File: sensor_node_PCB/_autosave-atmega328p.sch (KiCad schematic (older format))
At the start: 11 parts, among them U5 ATmega328P-AU, Y1 Crystal

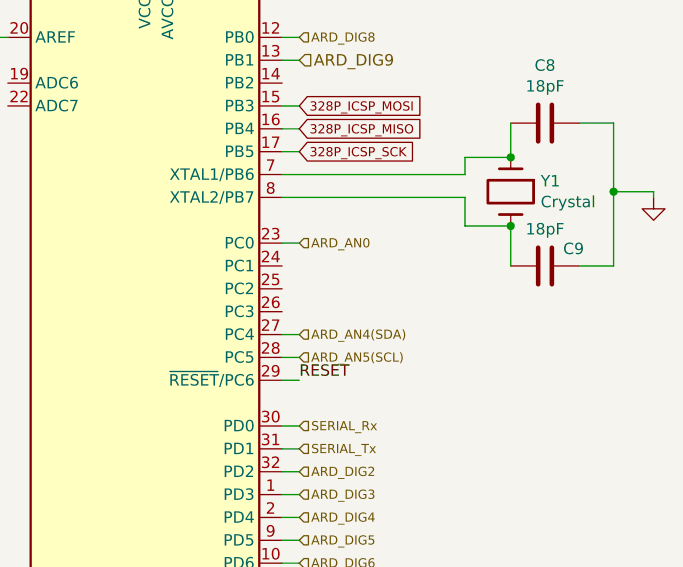
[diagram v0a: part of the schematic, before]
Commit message: made term block silk invisible
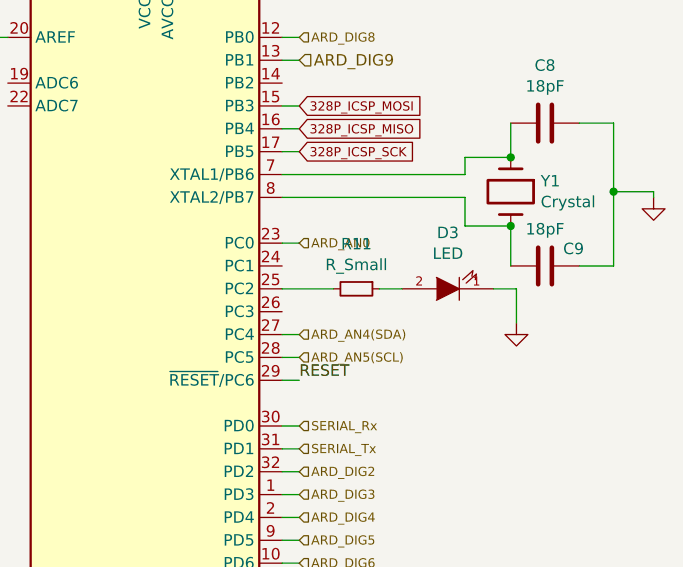
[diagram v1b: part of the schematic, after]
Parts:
- added D3: LED, LED_SMD:LED_0603_1608Metric, symbol Arduino_Uno_R3_From_Scratch-rescue:LED
- added R11: R_Small, LED_SMD:LED_0603_1608Metric, symbol Device:R_Small
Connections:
- net GND: now also D3.1 (K)
- net at U5.25 (PC2): now also R11.2
- new net: D3.2 (A), R11.1
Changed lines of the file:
@@
 Wire Wire Line
 	3625 2050 5325 2050
+$Comp
+L Device:R_Small R11
+U 1 1 5FF88592
+P 8075 4325
+F 0 "R11" V 7879 4325 50  0000 C CNN
+F 1 "R_Small" V 7970 4325 50  0000 C CNN
+F 2 "LED_SMD:LED_0603_1608Metric" H 8075 4325 50  0001 C CNN
+F 3 "~" H 8075 4325 50  0001 C CNN
+	1    8075 4325
+	0    1    1    0
+$EndComp
+$Comp
+L Arduino_Uno_R3_From_Scratch-rescue:LED D3
+U 1 1 5FF88C19
+P 8475 4325
+F 0 "D3" H 8475 4080 50  0000 C CNN
+F 1 "LED" H 8475 4171 50  0000 C CNN
+F 2 "LED_SMD:LED_0603_1608Metric" H 8475 4325 60  0001 C CNN
+F 3 "" H 8475 4325 60  0000 C CNN
+	1    8475 4325
+	-1   0    0    1
+$EndComp
+$Comp
+L Arduino_Uno_R3_From_Scratch-rescue:GND #PWR0147
+U 1 1 5FF893A9
+P 8775 4475
+F 0 "#PWR0147" H 8775 4475 30  0001 C CNN
+F 1 "GND" H 8775 4405 30  0001 C CNN
+F 2 "~" H 8775 4475 60  0000 C CNN
+F 3 "~" H 8775 4475 60  0000 C CNN
+F 4 "ANY" H 8775 4475 60  0001 C CNN "Source"
+F 5 "N" H 8775 4475 60  0001 C CNN "Critical"
+F 6 "~" H 8775 4475 60  0001 C CNN "Notes"
+	1    8775 4475
+	1    0    0    -1
+$EndComp
+Wire Wire Line
+	7750 4325 7975 4325
+Wire Wire Line
+	8175 4325 8275 4325
+Wire Wire Line
+	8675 4325 8775 4325
+Wire Wire Line
+	8775 4325 8775 4475
 $EndSCHEMATC
